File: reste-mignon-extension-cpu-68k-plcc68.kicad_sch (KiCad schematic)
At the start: 3 parts, among them J1 RESTE_MIGNON_CPU_CONNECTOR_A, J2 RESTE_MIGNON_CPU_CONNECTOR_B, U1 MC68000_PLCC_68_PHY

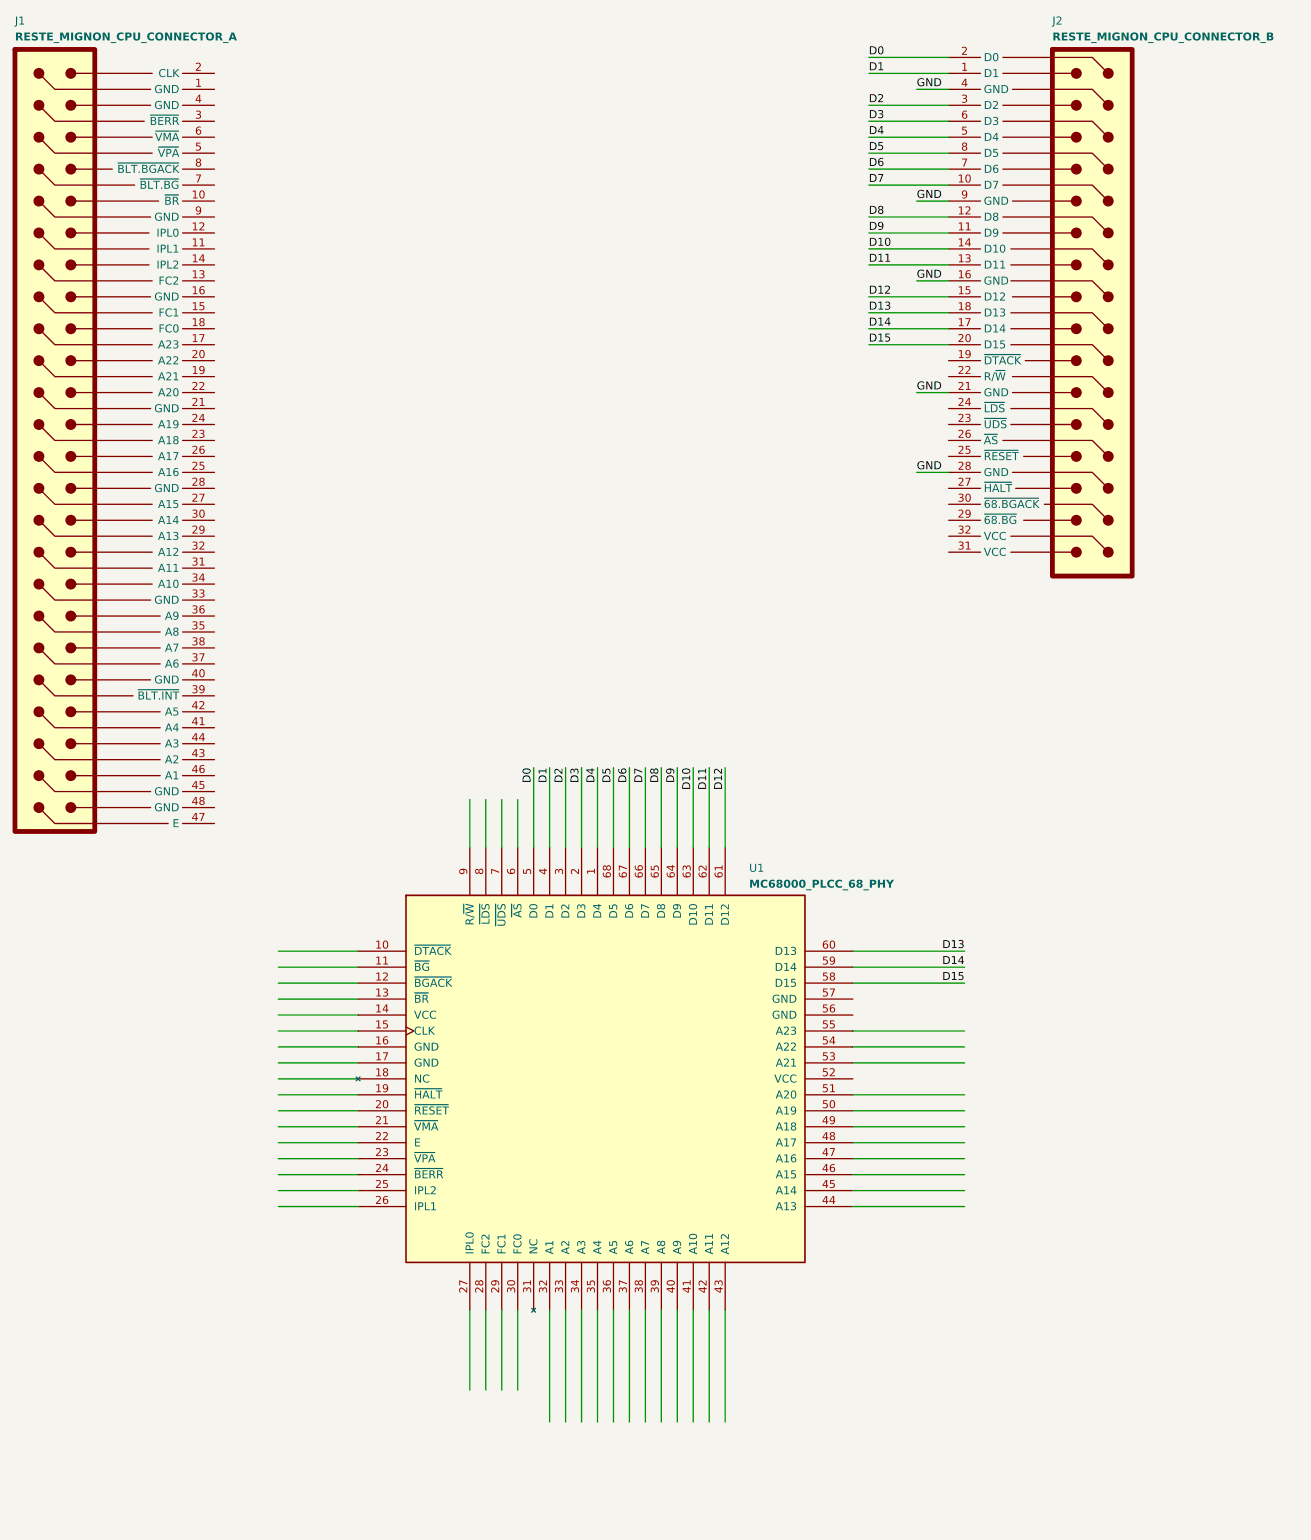
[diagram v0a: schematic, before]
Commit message: done main wiring, remaining pull-ups
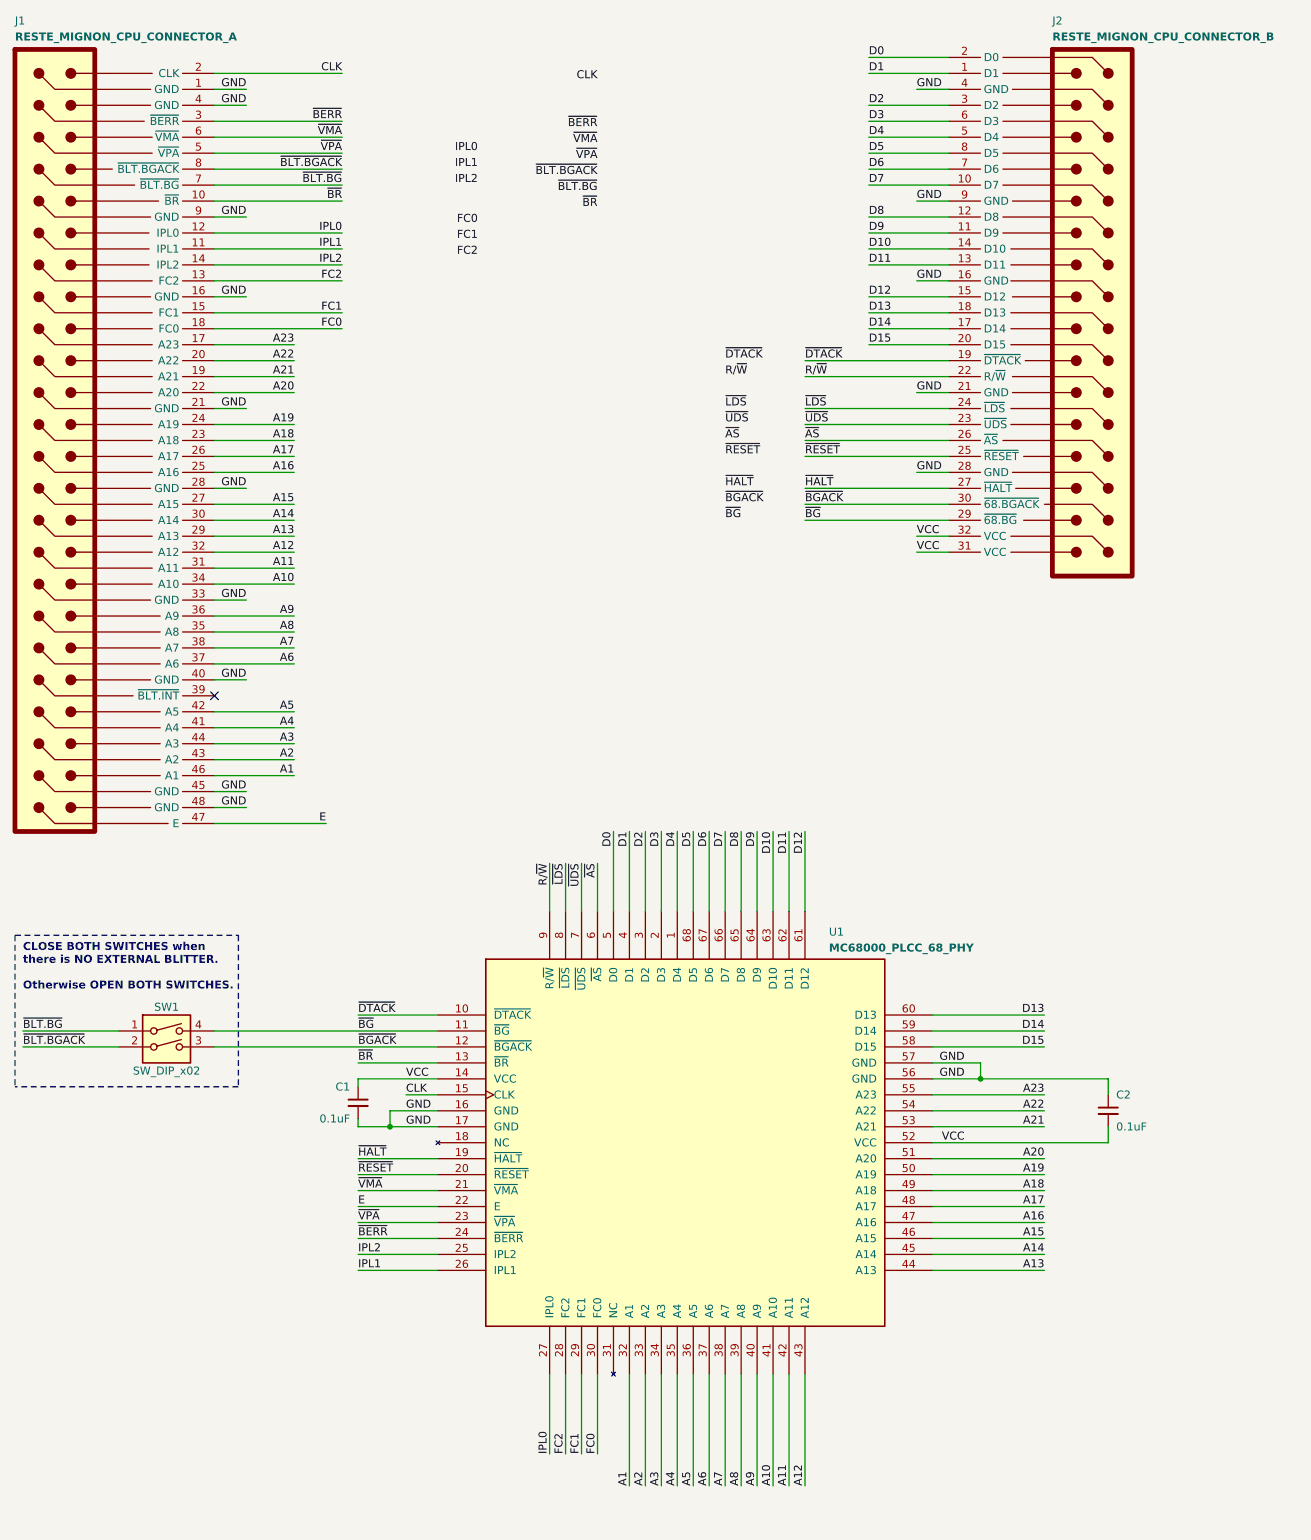
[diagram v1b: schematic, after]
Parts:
- added C1, C2: 0.1uF, symbol Device:C_Small
- added SW1: SW_DIP_x02, symbol Switch:SW_DIP_x02
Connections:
- net GND: now also J1.1 (GND), J1.16 (GND), J1.21 (GND), J1.28 (GND), J1.33 (GND), J1.4 (GND), J1.40 (GND), J1.45 (GND), J1.48 (GND), J1.9 (GND), U1.16 (GND), U1.17 (GND), U1.56 (GND), U1.57 (GND), C1.2, C2.1
- net ~{BR}: now reaches J1.10 (~{BR})
- net ~{BR}: now also U1.13 (~{BR})
- net IPL1: now reaches J1.11 (IPL1)
- net IPL1: now also U1.26 (IPL1)
- net IPL0: now reaches J1.12 (IPL0)
- net IPL0: now also U1.27 (IPL0)
- net FC2: now reaches J1.13 (FC2)
- net FC2: now also U1.28 (FC2)
- net IPL2: now reaches J1.14 (IPL2)
- net IPL2: now also U1.25 (IPL2)
- net FC1: now reaches J1.15 (FC1)
- net FC1: now also U1.29 (FC1)
- net A23: now reaches J1.17 (A23)
- net A23: now also U1.55 (A23)
- net FC0: now reaches J1.18 (FC0)
- net FC0: now also U1.30 (FC0)
- net A21: now reaches J1.19 (A21)
- net A21: now also U1.53 (A21)
- net CLK: now reaches J1.2 (CLK)
- net CLK: now also U1.15 (CLK)
- net A22: now reaches J1.20 (A22)
- net A22: now also U1.54 (A22)
- net A20: now reaches J1.22 (A20)
- net A20: now also U1.51 (A20)
- net A18: now reaches J1.23 (A18)
- net A18: now also U1.49 (A18)
- net A19: now reaches J1.24 (A19)
- net A19: now also U1.50 (A19)
- net A16: now reaches J1.25 (A16)
- net A16: now also U1.47 (A16)
- net A17: now reaches J1.26 (A17)
- net A17: now also U1.48 (A17)
- net A15: now reaches J1.27 (A15)
- net A15: now also U1.46 (A15)
- net A13: now reaches J1.29 (A13)
- net A13: now also U1.44 (A13)
- net ~{BERR}: now reaches J1.3 (~{BERR})
- net ~{BERR}: now also U1.24 (~{BERR})
- net A14: now reaches J1.30 (A14)
- net A14: now also U1.45 (A14)
- net A11: now reaches J1.31 (A11)
- net A11: now also U1.42 (A11)
- net A12: now reaches J1.32 (A12)
- net A12: now also U1.43 (A12)
- net A10: now reaches J1.34 (A10)
- net A10: now also U1.41 (A10)
- net A8: now reaches J1.35 (A8)
- net A8: now also U1.39 (A8)
- net A9: now reaches J1.36 (A9)
- net A9: now also U1.40 (A9)
- net A6: now reaches J1.37 (A6)
- net A6: now also U1.37 (A6)
- net A7: now reaches J1.38 (A7)
- net A7: now also U1.38 (A7)
- net A4: now reaches J1.41 (A4)
- net A4: now also U1.35 (A4)
- net A5: now reaches J1.42 (A5)
- net A5: now also U1.36 (A5)
- net A2: now reaches J1.43 (A2)
- net A2: now also U1.33 (A2)
- net A3: now reaches J1.44 (A3)
- net A3: now also U1.34 (A3)
- net A1: now reaches J1.46 (A1)
- net A1: now also U1.32 (A1)
- net E: now reaches J1.47 (E)
- net E: now also U1.22 (E)
- net ~{VPA}: now reaches J1.5 (~{VPA})
- net ~{VPA}: now also U1.23 (~{VPA})
- net ~{VMA}: now reaches J1.6 (~{VMA})
- net ~{VMA}: now also U1.21 (~{VMA})
- net ~{BLT.BG}: now reaches J1.7 (~{BLT.BG})
- net ~{BLT.BG}: now also SW1.1
- net ~{BLT.BGACK}: now reaches J1.8 (~{BLT.BGACK})
- net ~{BLT.BGACK}: now also SW1.2
- net ~{DTACK}: now reaches U1.10 (~{DTACK})
- net ~{DTACK}: now also J2.19 (~{DTACK})
- net ~{BG}: now reaches U1.11 (~{BG})
- net ~{BG}: now also J2.29 (~{68.BG}), SW1.4
- net ~{BGACK}: now reaches U1.12 (~{BGACK})
- net ~{BGACK}: now also J2.30 (~{68.BGACK}), SW1.3
- net VCC: now reaches U1.14 (VCC)
- net VCC: now also J2.31 (VCC), J2.32 (VCC), U1.52 (VCC), C1.1, C2.2
- net ~{HALT}: now reaches U1.19 (~{HALT})
- net ~{HALT}: now also J2.27 (~{HALT})
- net ~{RESET}: now reaches U1.20 (~{RESET})
- net ~{RESET}: now also J2.25 (~{RESET})
- net ~{AS}: now reaches U1.6 (~{AS})
- net ~{AS}: now also J2.26 (~{AS})
- net ~{UDS}: now reaches U1.7 (~{UDS})
- net ~{UDS}: now also J2.23 (~{UDS})
- net ~{LDS}: now reaches U1.8 (~{LDS})
- net ~{LDS}: now also J2.24 (~{LDS})
- net R/~{W}: now reaches U1.9 (R/~{W})
- net R/~{W}: now also J2.22 (R/~{W})
- no-connect marks 0 -> 1
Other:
- note added: "CLOSE BOTH SWITCHES when there is NO EXTERNAL BLITTER. Otherwise OPEN BOTH SWITCHES."
- moved on the sheet: U1

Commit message: done schematic
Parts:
- removed SW1: SW_DIP_x02, symbol Switch:SW_DIP_x02
- added JP1, JP2: (no value), symbol Jumper:SolderJumper_2_Bridged
- added R1, R2: 1K, symbol Device:R_Small_US
- added R3, R4, R5: 10K, symbol Device:R_Small_US
- added R6: 2K2, symbol Device:R_Small_US
- added R7: 4K7, symbol Device:R_Small_US
- added RN1: 8×1K2, Resistor_THT:R_Array_SIP9, symbol Device:R_Network08_US
- added RN2, RN3, RN4, RN5, RN6: 8×2K2, Resistor_THT:R_Array_SIP9, symbol Device:R_Network08_US
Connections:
- net A1: now also RN2.2 (R1)
- net A10: now also RN3.3 (R2)
- net A11: now also RN3.4 (R3)
- net A12: now also RN3.5 (R4)
- net A13: now also RN3.6 (R5)
- net A14: now also RN3.7 (R6)
- net A15: now also RN3.8 (R7)
- net A16: now also RN3.9 (R8)
- net A17: now also RN4.2 (R1)
- net A18: now also RN4.3 (R2)
- net A19: now also RN4.4 (R3)
- net A2: now also RN2.3 (R2)
- net A20: now also RN4.5 (R4)
- net A21: now also RN4.6 (R5)
- net A22: now also RN4.7 (R6)
- net A23: now also RN4.8 (R7)
- net A3: now also RN2.4 (R3)
- net A4: now also RN2.5 (R4)
- net A5: now also RN2.6 (R5)
- net A6: now also RN2.7 (R6)
- net A7: now also RN2.8 (R7)
- net A8: now also RN2.9 (R8)
- net A9: now also RN3.2 (R1)
- net D0: now also RN5.2 (R1)
- net D1: now also RN5.3 (R2)
- net D10: now also RN6.4 (R3)
- net D11: now also RN6.5 (R4)
- net D12: now also RN6.6 (R5)
- net D13: now also RN6.7 (R6)
- net D14: now also RN6.8 (R7)
- net D15: now also RN6.9 (R8)
- net D2: now also RN5.4 (R3)
- net D3: now also RN5.5 (R4)
- net D4: now also RN5.6 (R5)
- net D5: now also RN5.7 (R6)
- net D6: now also RN5.8 (R7)
- net D7: now also RN5.9 (R8)
- net D8: now also RN6.2 (R1)
- net D9: now also RN6.3 (R2)
- net FC0: now also R5.1
- net FC1: now also R4.1
- net FC2: now also R3.1
- net R/~{W}: now also RN1.6 (R5)
- net VCC: now also R1.2, R2.2, R3.2, R4.2, R5.2, R6.2, R7.2, RN1.1 (common), RN2.1 (common), RN3.1 (common), RN4.1 (common), RN5.1 (common), RN6.1 (common)
- net ~{AS}: now also RN1.9 (R8)
- net ~{BERR}: now also RN1.3 (R2)
- net ~{BGACK}: now also JP2.2 (B), RN1.4 (R3)
- net ~{BG}: now also JP1.2 (B)
- net ~{BLT.BGACK}: now also JP2.1 (A)
- net ~{BLT.BG}: now also JP1.1 (A)
- net ~{BR}: now also RN1.5 (R4)
- net ~{DTACK}: now also R1.1
- net ~{HALT}: now also RN1.2 (R1)
- net ~{LDS}: now also RN1.7 (R6)
- net ~{RESET}: now also R2.1
- net ~{UDS}: now also RN1.8 (R7)
- net ~{VMA}: now also R7.1
- net ~{VPA}: now also R6.1
- no-connect marks 1 -> 2
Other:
- note added: "BRIDGED when there is NO EXTERNAL BLITTER. Otherwise CUT BOTH."
- note added: "No pull up ?"
- note removed: "CLOSE BOTH SWITCHES when there is NO EXTERNAL BLITTER. Otherwise OPEN BOTH SWITCHES."

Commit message: done footprint association, DRC
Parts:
- C1, C2: footprint (none) -> commons_passives_THT:Passive_THT_capacitor_mlcc_W2.54mm_L5.08mm
- JP1: footprint (none) -> Connector_PinHeader_2.54mm:PinHeader_2x24_P2.54mm_Vertical
- JP2: footprint (none) -> Connector_PinHeader_2.54mm:PinHeader_2x16_P2.54mm_Vertical
- R1, R2, R3, R4, R5, R6, R7: footprint (none) -> commons_passives_THT:Passive_THT_resistor_W2.54mm_L10.16mm
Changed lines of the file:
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@@
+    (stroke (width 0) (type default))
+  )
+  (wire (pts (xy 16.51 256.54) (xy 29.21 256.54))
     (stroke (width 0) (type default))
   )
@@
   )
   (wire (pts (xy 48.26 50.8) (xy 68.58 50.8))
+    (stroke (width 0) (type default))
+  )
+  (wire (pts (xy 16.51 246.38) (xy 29.21 246.38))
     (stroke (width 0) (type default))
   )
@@
     (effects (font (size 1.27 1.27)) (justify left bottom))
   )
+  (label "VCC" (at 16.51 246.38 0) (fields_autoplaced)
+    (effects (font (size 1.27 1.27)) (justify left bottom))
+  )
   (label "GND" (at 78.74 190.5 0) (fields_autoplaced)
     (effects (font (size 1.27 1.27)) (justify left bottom))
@@
   )
   (label "GND" (at 160.02 27.94 0) (fields_autoplaced)
+    (effects (font (size 1.27 1.27)) (justify left bottom))
+  )
+  (label "GND" (at 16.51 256.54 0) (fields_autoplaced)
     (effects (font (size 1.27 1.27)) (justify left bottom))
   )
@@
       (effects (font (size 1.27 1.27)) (justify left))
     )
-    (property "Footprint" "" (at 190.5 190.5 0)
+    (property "Footprint" "commons_passives_THT:Passive_THT_capacitor_mlcc_W2.54mm_L5.08mm" (at 190.5 190.5 0)
       (effects (font (size 1.27 1.27)) hide)
     )
@@
         (path "/5ae9712c-56a4-4baf-99ee-c0a0e97d4775"
           (reference "C2") (unit 1)
+        )
+      )
+    )
+  )
+  (symbol (lib_id "power:PWR_FLAG") (at 29.21 256.54 0) (unit 1)
+    (in_bom yes) (on_board yes) (dnp no)
+    (property "Reference" "#FLG01" (at 29.21 254.635 0)
+      (effects (font (size 1.27 1.27)) hide)
+    )
+    (property "Value" "PWR_FLAG" (at 29.21 252.73 0)
+      (effects (font (size 1.27 1.27)))
+    )
+    (property "Footprint" "" (at 29.21 256.54 0)
+      (effects (font (size 1.27 1.27)) hide)
+    )
+    (property "Datasheet" "~" (at 29.21 256.54 0)
+      (effects (font (size 1.27 1.27)) hide)
+    )
+    (pin "1")
+    (instances
+      (project "reste-mignon-extension-cpu-68k-plcc68"
+        (path "/5ae9712c-56a4-4baf-99ee-c0a0e97d4775"
+          (reference "#FLG01") (unit 1)
         )
       )
@@
       (effects (font (size 1.27 1.27)) (justify right))
     )
-    (property "Footprint" "" (at 149.86 116.84 0)
+    (property "Footprint" "commons_passives_THT:Passive_THT_resistor_W2.54mm_L10.16mm" (at 149.86 116.84 0)
       (effects (font (size 1.27 1.27)) hide)
     )
@@
       (effects (font (size 1.27 1.27)) (justify right))
     )
-    (property "Footprint" "" (at 149.86 111.76 0)
+    (property "Footprint" "commons_passives_THT:Passive_THT_resistor_W2.54mm_L10.16mm" (at 149.86 111.76 0)
       (effects (font (size 1.27 1.27)) hide)
     )
@@
       (effects (font (size 1.27 1.27)) (justify left))
     )
-    (property "Footprint" "" (at 40.64 177.8 0)
+    (property "Footprint" "Connector_PinHeader_2.54mm:PinHeader_2x24_P2.54mm_Vertical" (at 40.64 177.8 0)
       (effects (font (size 1.27 1.27)) hide)
     )
@@
       (effects (font (size 1.27 1.27)) (justify right))
     )
-    (property "Footprint" "" (at 149.86 121.92 0)
+    (property "Footprint" "commons_passives_THT:Passive_THT_resistor_W2.54mm_L10.16mm" (at 149.86 121.92 0)
       (effects (font (size 1.27 1.27)) hide)
     )
@@
       (effects (font (size 1.27 1.27)) (justify right))
     )
-    (property "Footprint" "" (at 149.86 119.38 0)
+    (property "Footprint" "commons_passives_THT:Passive_THT_resistor_W2.54mm_L10.16mm" (at 149.86 119.38 0)
       (effects (font (size 1.27 1.27)) hide)
     )
@@
       (effects (font (size 1.27 1.27)) (justify right))
     )
-    (property "Footprint" "" (at 71.12 189.23 0)
+    (property "Footprint" "commons_passives_THT:Passive_THT_capacitor_mlcc_W2.54mm_L5.08mm" (at 71.12 189.23 0)
       (effects (font (size 1.27 1.27)) hide)
     )
@@
         (path "/5ae9712c-56a4-4baf-99ee-c0a0e97d4775"
           (reference "C1") (unit 1)
+        )
+      )
+    )
+  )
+  (symbol (lib_id "power:PWR_FLAG") (at 29.21 246.38 0) (unit 1)
+    (in_bom yes) (on_board yes) (dnp no)
+    (property "Reference" "#FLG02" (at 29.21 244.475 0)
+      (effects (font (size 1.27 1.27)) hide)
+    )
+    (property "Value" "PWR_FLAG" (at 29.21 242.57 0)
+      (effects (font (size 1.27 1.27)))
+    )
+    (property "Footprint" "" (at 29.21 246.38 0)
+      (effects (font (size 1.27 1.27)) hide)
+    )
+    (property "Datasheet" "~" (at 29.21 246.38 0)
+      (effects (font (size 1.27 1.27)) hide)
+    )
+    (pin "1")
+    (instances
+      (project "reste-mignon-extension-cpu-68k-plcc68"
+        (path "/5ae9712c-56a4-4baf-99ee-c0a0e97d4775"
+          (reference "#FLG02") (unit 1)
         )
       )
@@
       (effects (font (size 1.27 1.27)) (justify left))
     )
-    (property "Footprint" "" (at 40.64 180.34 0)
+    (property "Footprint" "Connector_PinHeader_2.54mm:PinHeader_2x16_P2.54mm_Vertical" (at 40.64 180.34 0)
       (effects (font (size 1.27 1.27)) hide)
     )
@@
       (effects (font (size 1.27 1.27)) (justify right))
     )
-    (property "Footprint" "" (at 149.86 109.22 0)
+    (property "Footprint" "commons_passives_THT:Passive_THT_resistor_W2.54mm_L10.16mm" (at 149.86 109.22 0)
       (effects (font (size 1.27 1.27)) hide)
     )
@@
       (effects (font (size 1.27 1.27)) (justify right))
     )
-    (property "Footprint" "" (at 149.86 114.3 0)
+    (property "Footprint" "commons_passives_THT:Passive_THT_resistor_W2.54mm_L10.16mm" (at 149.86 114.3 0)
       (effects (font (size 1.27 1.27)) hide)
     )
@@
       (effects (font (size 1.27 1.27)) (justify right))
     )
-    (property "Footprint" "" (at 149.86 124.46 0)
-      (effects (font (size 1.27 1.27)) hide)
-    )
+    (property "Footprint" "commons_passives_THT:Passive_THT_resistor_W2.54mm_L10.16mm" (at 149.86 124.46 0)
+      (effects (font (size 1.27 1.27)) hide)
+    )
